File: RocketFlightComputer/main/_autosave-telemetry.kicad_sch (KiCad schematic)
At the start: 3 parts

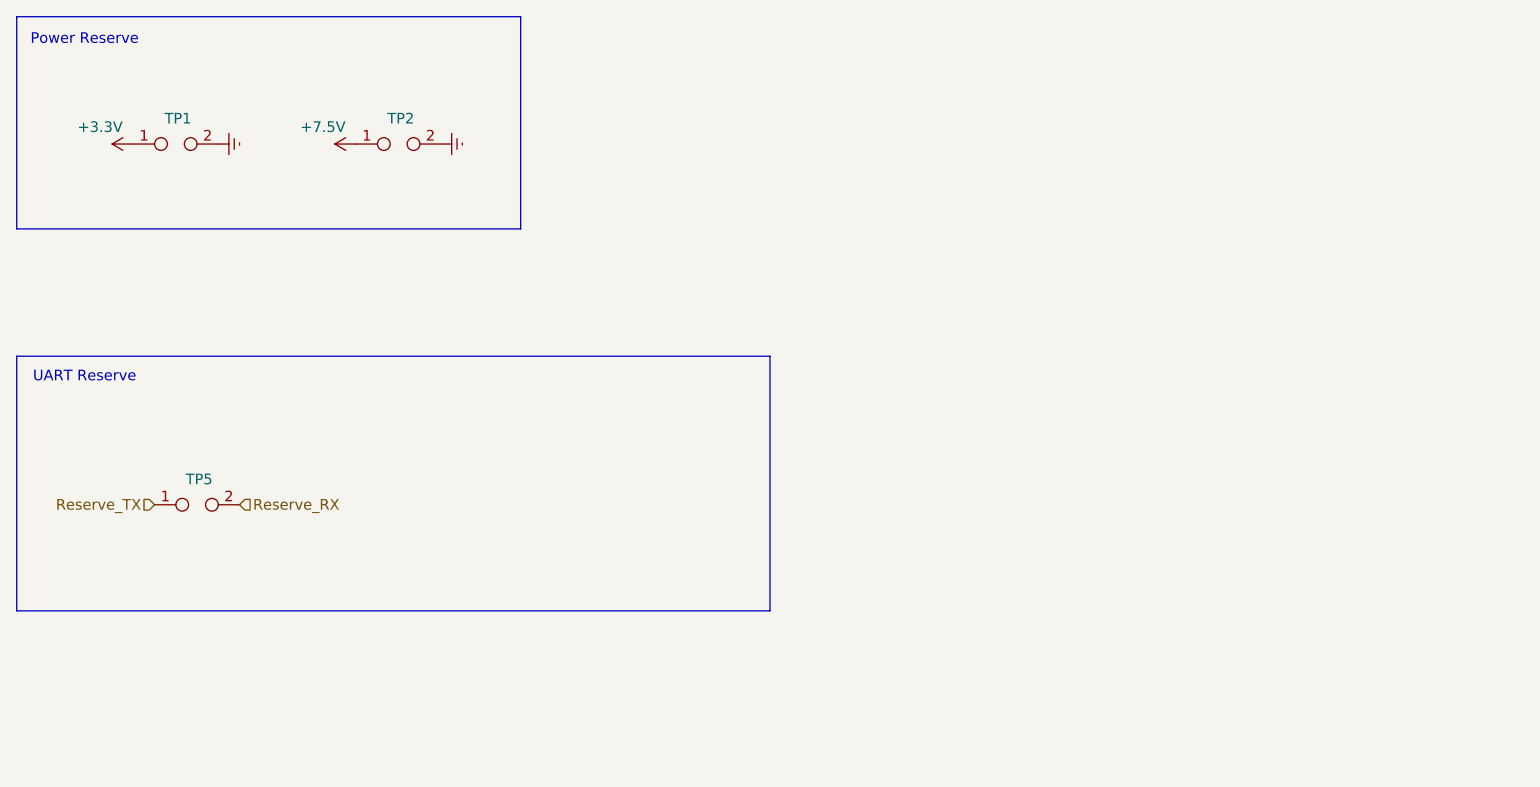
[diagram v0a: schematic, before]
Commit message: First iteration of layout finished, we could call this v0, congratulations! Need an expert to state if layer 4 and layer 3 interations are ok (pwm/ psram/i2c/uart vs power plane 7.5v and 3.3v )
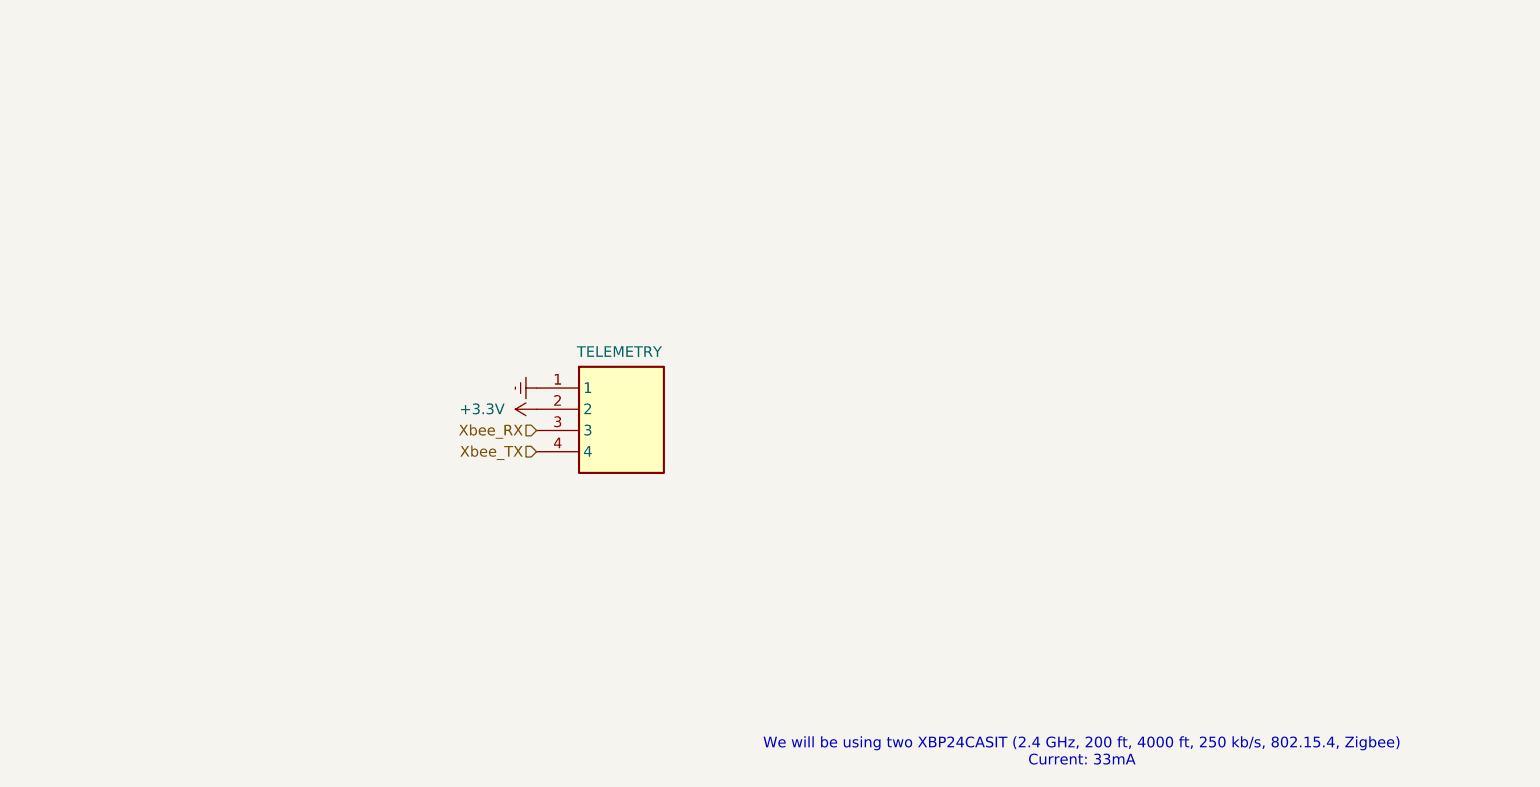
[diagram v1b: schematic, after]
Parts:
- removed TP1, TP2, TP5: TestPoint_2Pole, TestPoint:TestPoint_2Pads_Pitch2.54mm_Drill0.8mm, symbol Connector:TestPoint_2Pole
- added S4B-PH-K-S_LF__SN_1: TELEMETRY, Connector_JST:JST_GH_BM04B-GHS-TBT_1x04-1MP_P1.25mm_Vertical, symbol B3P-VH_LF__SN_:S4B-PH-K-S_LF__SN_
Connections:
- net +3.3V: now also S4B-PH-K-S_LF__SN_1.2
- net GNDREF: now also S4B-PH-K-S_LF__SN_1.1
- new net Xbee_RX: S4B-PH-K-S_LF__SN_1.3
- new net Xbee_TX: S4B-PH-K-S_LF__SN_1.4
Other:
- note added: "We will be using two XBP24CASIT (2.4 GHz, 200 ft, 4000 ft, 250 kb/s, 802.15.4, Zigbee) Current: 33mA"
- note removed: "Power Reserve"
- note removed: "UART Reserve"
